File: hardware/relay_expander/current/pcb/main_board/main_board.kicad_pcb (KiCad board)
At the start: 2 copper layers, 130 x 85 mm, 83 parts, among them J1 Conn_01x07_Socket, J10 Screw_Terminal_01x02, J11 Screw_Terminal_01x02, J12 Screw_Terminal_01x02, J13 Screw_Terminal_01x02, J14 Screw_Terminal_01x02, J15 Screw_Terminal_01x02, J16 Screw_Terminal_01x02, J2 Conn_01x07_Socket, J3 Conn_01x02_Socket, J4 Screw_Terminal_01x02, J5 Screw_Terminal_01x02, J6 Screw_Terminal_01x02, J7 Screw_Terminal_01x02, J8 Screw_Terminal_01x02, J9 Screw_Terminal_01x02, K1 SANYOU_SRD_Form_C, K2 SANYOU_SRD_Form_C, K3 SANYOU_SRD_Form_C, K4 SANYOU_SRD_Form_C, K5 SANYOU_SRD_Form_C, K6 SANYOU_SRD_Form_C, K7 SANYOU_SRD_Form_C, K8 SANYOU_SRD_Form_C, U1 MCP23017x-x-SO, U2 ULN2803A, U3 TCMT4100, U4 TCMT4100, U5 TSR1-2433E

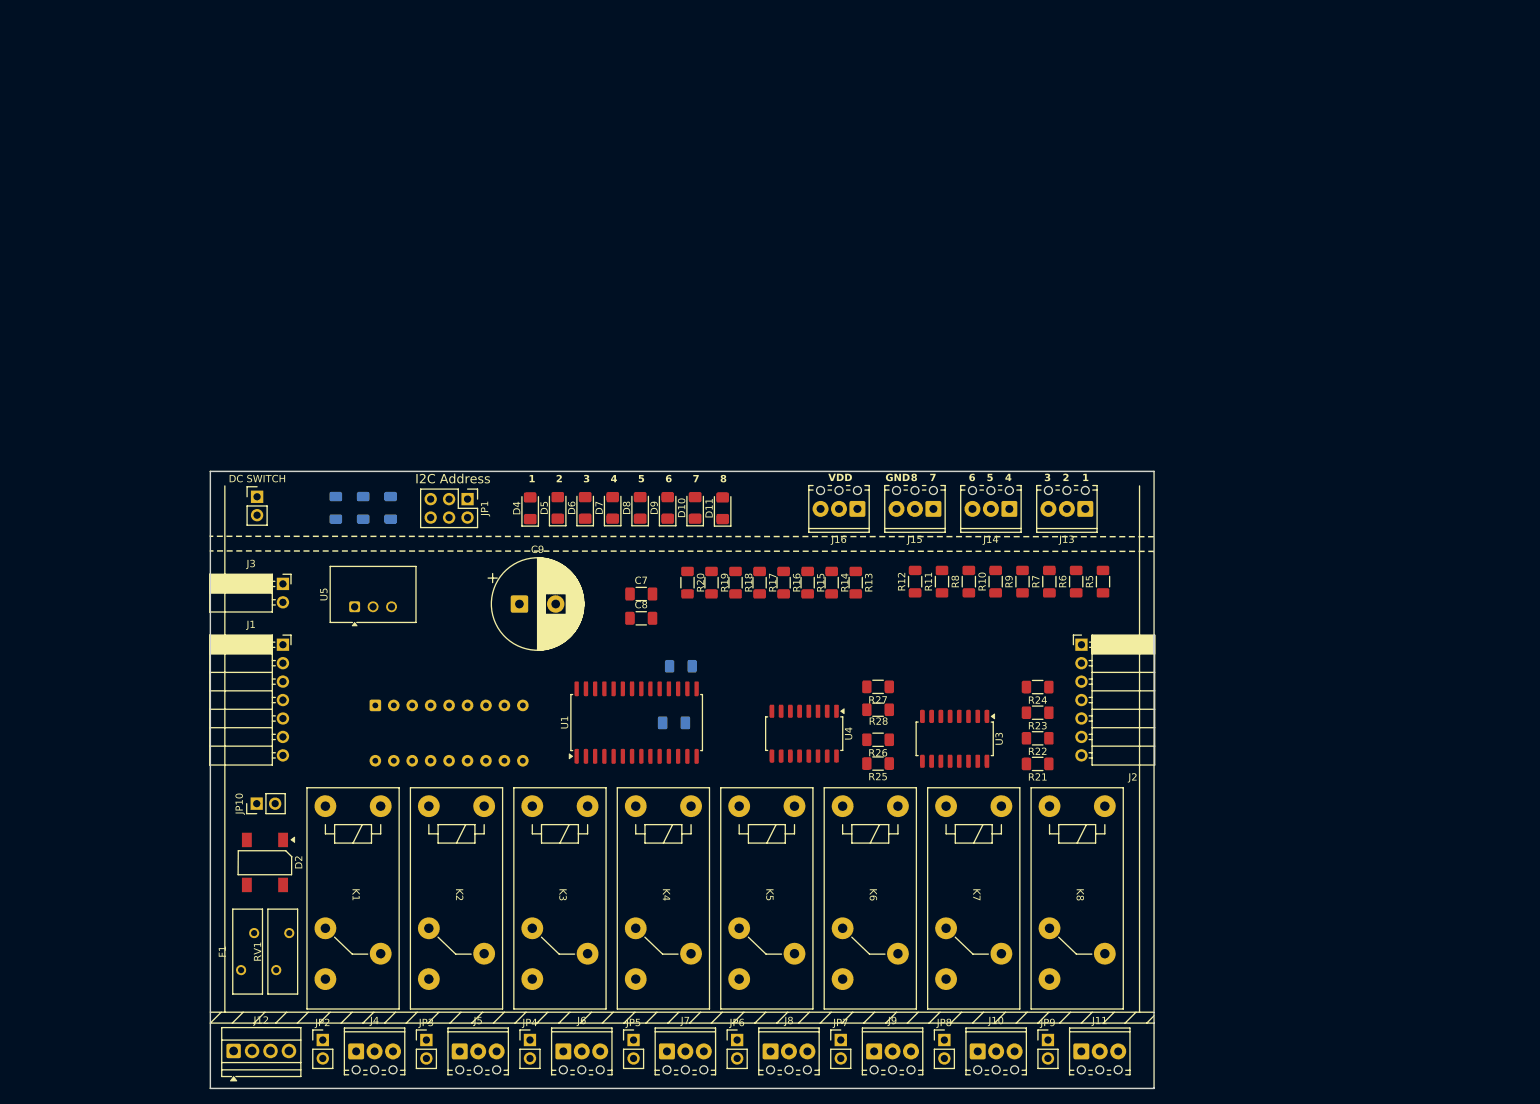
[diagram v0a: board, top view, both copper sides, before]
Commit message: [ADD] lauout for relay expander pcb
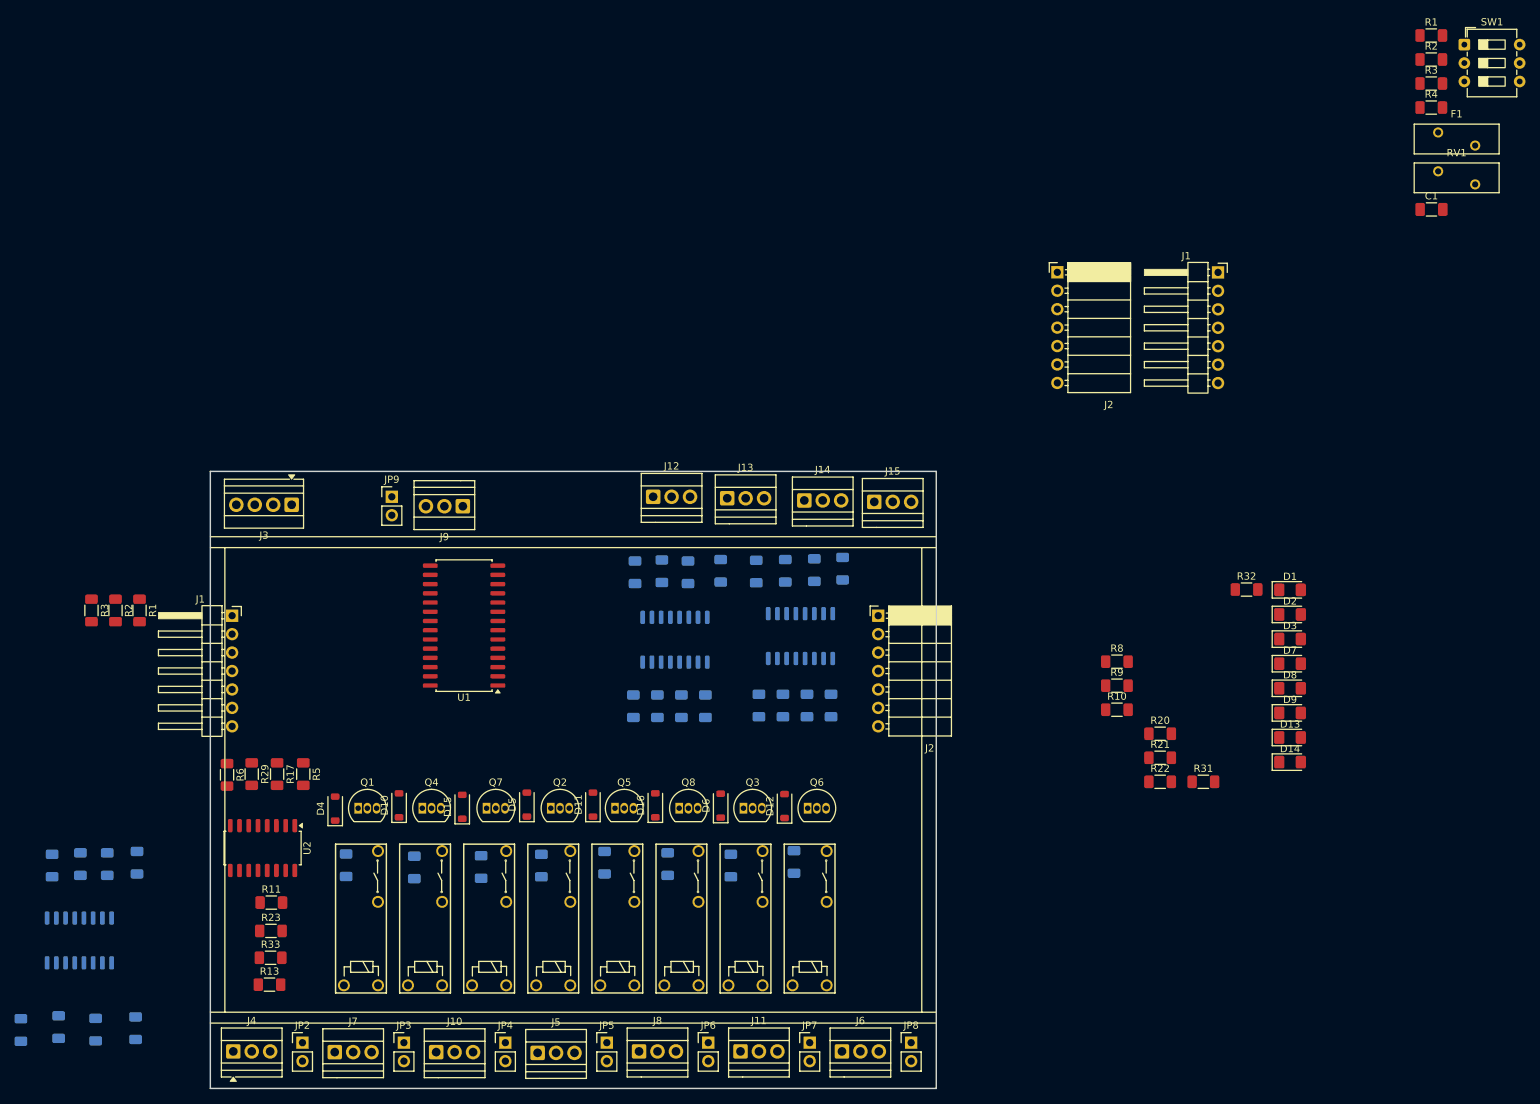
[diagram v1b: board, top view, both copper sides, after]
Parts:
- removed C7, C8: 22uF, Capacitor_SMD:C_1206_3216Metric_Pad1.33x1.80mm_HandSolder
- removed C9: 1000uF, Capacitor_THT:CP_Radial_D12.5mm_P5.00mm
- removed J16: Screw_Terminal_01x02, Project_Parts_Footprints_Lib:TerminalBlock_Phoenix_MPT-0,5-3-2.54_1x03_P2.54mm_Horizontal
- removed JP1: ~, Connector_PinHeader_2.54mm:PinHeader_2x03_P2.54mm_Vertical
- removed JP10: DC IN 6 - 36V, Connector_PinHeader_2.54mm:PinHeader_1x02_P2.54mm_Vertical
- removed JP13: DC SWITCH, Connector_PinHeader_2.54mm:PinHeader_1x02_P2.54mm_Vertical
- removed the R1 at (109.8, 57.5)
- removed the R2 at (106.1, 57.5)
- removed the R3 at (102.3, 57.5)
- added D1: LED, LED_SMD:LED_1206_3216Metric_Pad1.42x1.75mm_HandSolder, F.Cu at (233.7, 68.8)
- added D12: 1N4148, Diode_SMD:D_SOD-123, F.Cu at (164.1, 98.6)
- added D13: LED, LED_SMD:LED_1206_3216Metric_Pad1.42x1.75mm_HandSolder, F.Cu at (233.7, 89.2)
- added D14: LED, LED_SMD:LED_1206_3216Metric_Pad1.42x1.75mm_HandSolder, F.Cu at (233.7, 92.5)
- added D15: 1N4148, Diode_SMD:D_SOD-123, F.Cu at (119.7, 98.7)
- added D16: 1N4148, Diode_SMD:D_SOD-123, F.Cu at (146.3, 98.5)
- added D3: LED, LED_SMD:LED_1206_3216Metric_Pad1.42x1.75mm_HandSolder, F.Cu at (233.7, 75.6)
- added J1: Conn_01x07_Socket, homeautomation_core:PinHeader_1x07_P2.54mm_Horizontal_left, F.Cu at (223.8, 32.7)
- added J2: Conn_01x07_Socket, homeautomation_core:PinSocket_1x07_P2.54mm_Horizontal_Right, F.Cu at (201.7, 32.7)
- added Q1: BC548, Package_TO_SOT_THT:TO-92_Inline, F.Cu at (105.4, 98.9)
- added Q2: BC548, Package_TO_SOT_THT:TO-92_Inline, F.Cu at (131.9, 98.9)
- added Q3: BC548, Package_TO_SOT_THT:TO-92_Inline, F.Cu at (158.4, 98.9)
- added Q4: BC548, Package_TO_SOT_THT:TO-92_Inline, F.Cu at (114.2, 98.9)
- added Q5: BC548, Package_TO_SOT_THT:TO-92_Inline, F.Cu at (140.7, 98.9)
- added Q6: BC548, Package_TO_SOT_THT:TO-92_Inline, F.Cu at (167.3, 98.9)
- added Q7: BC548, Package_TO_SOT_THT:TO-92_Inline, F.Cu at (123.1, 98.9)
- added Q8: BC548, Package_TO_SOT_THT:TO-92_Inline, F.Cu at (149.6, 98.9)
- added R1: 10k, Resistor_SMD:R_1206_3216Metric_Pad1.30x1.75mm_HandSolder, F.Cu at (75.2, 71.7)
- added R1: 10k, Resistor_SMD:R_1206_3216Metric_Pad1.30x1.75mm_HandSolder, F.Cu at (253.2, -7.54)
- added R2: 10k, Resistor_SMD:R_1206_3216Metric_Pad1.30x1.75mm_HandSolder, F.Cu at (253.2, -4.24)
- added R2: 10k, Resistor_SMD:R_1206_3216Metric_Pad1.30x1.75mm_HandSolder, F.Cu at (71.9, 71.7)
- added R29: R470, Resistor_SMD:R_1206_3216Metric_Pad1.30x1.75mm_HandSolder, F.Cu at (90.7, 94.2)
- added R3: 10k, Resistor_SMD:R_1206_3216Metric_Pad1.30x1.75mm_HandSolder, F.Cu at (68.6, 71.7)
- added R3: 10k, Resistor_SMD:R_1206_3216Metric_Pad1.30x1.75mm_HandSolder, F.Cu at (253.2, -0.93)
- added R30: R470, Resistor_SMD:R_1206_3216Metric_Pad1.30x1.75mm_HandSolder, B.Cu at (67.1, 106.6)
- added R31: 1k, Resistor_SMD:R_1206_3216Metric_Pad1.30x1.75mm_HandSolder, F.Cu at (221.8, 95.3)
- added R32: 1k, Resistor_SMD:R_1206_3216Metric_Pad1.30x1.75mm_HandSolder, F.Cu at (227.7, 68.8)
- added R33: R4,7k, Resistor_SMD:R_1206_3216Metric_Pad1.30x1.75mm_HandSolder, F.Cu at (93.3, 119.5)
- added R34: R10k, Resistor_SMD:R_1206_3216Metric_Pad1.30x1.75mm_HandSolder, B.Cu at (122.3, 107.0)
- added R35: R4,7k, Resistor_SMD:R_1206_3216Metric_Pad1.30x1.75mm_HandSolder, B.Cu at (64.1, 129.1)
- added R36: R10k, Resistor_SMD:R_1206_3216Metric_Pad1.30x1.75mm_HandSolder, B.Cu at (139.3, 106.4)
- added R37: 1k, Resistor_SMD:R_1206_3216Metric_Pad1.30x1.75mm_HandSolder, B.Cu at (143.5, 66.4)
- added R38: 1k, Resistor_SMD:R_1206_3216Metric_Pad1.30x1.75mm_HandSolder, B.Cu at (147.2, 66.2)
- added R39: 1k, Resistor_SMD:R_1206_3216Metric_Pad1.30x1.75mm_HandSolder, B.Cu at (150.8, 66.4)
- added R40: 1k, Resistor_SMD:R_1206_3216Metric_Pad1.30x1.75mm_HandSolder, B.Cu at (155.3, 66.2)
- added R41: 1k, Resistor_SMD:R_1206_3216Metric_Pad1.30x1.75mm_HandSolder, B.Cu at (160.2, 66.3)
- added R42: 1k, Resistor_SMD:R_1206_3216Metric_Pad1.30x1.75mm_HandSolder, B.Cu at (164.2, 66.2)
- added R43: 1k, Resistor_SMD:R_1206_3216Metric_Pad1.30x1.75mm_HandSolder, B.Cu at (168.2, 66.1)
- added R44: 1k, Resistor_SMD:R_1206_3216Metric_Pad1.30x1.75mm_HandSolder, B.Cu at (172.1, 65.9)
- added R45: 10k, Resistor_SMD:R_1206_3216Metric_Pad1.30x1.75mm_HandSolder, B.Cu at (143.3, 84.8)
- added R46: 10k, Resistor_SMD:R_1206_3216Metric_Pad1.30x1.75mm_HandSolder, B.Cu at (146.6, 84.8)
- added R47: 10k, Resistor_SMD:R_1206_3216Metric_Pad1.30x1.75mm_HandSolder, B.Cu at (149.9, 84.8)
- added R48: 10k, Resistor_SMD:R_1206_3216Metric_Pad1.30x1.75mm_HandSolder, B.Cu at (153.2, 84.8)
- added R49: 10k, Resistor_SMD:R_1206_3216Metric_Pad1.30x1.75mm_HandSolder, B.Cu at (160.6, 84.8)
- added R50: 10k, Resistor_SMD:R_1206_3216Metric_Pad1.30x1.75mm_HandSolder, B.Cu at (163.9, 84.8)
- added R51: 10k, Resistor_SMD:R_1206_3216Metric_Pad1.30x1.75mm_HandSolder, B.Cu at (167.2, 84.8)
- added R52: 10k, Resistor_SMD:R_1206_3216Metric_Pad1.30x1.75mm_HandSolder, B.Cu at (170.5, 84.8)
- added SW1: SW_DIP_x03, Button_Switch_THT:SW_DIP_SPSTx03_Slide_6.7x9.18mm_W7.62mm_P2.54mm_LowProfile, F.Cu at (257.7, -6.29)
- C1, R4: moved to F.Cu
- D10, D11, D4, D5, D6: value LED -> 1N4148; footprint LED_SMD:LED_1206_3216Metric_Pad1.42x1.75mm_HandSolder -> Diode_SMD:D_SOD-123
- D2: value DB157S -> LED; footprint Wojtek_lib_footprints:DB157S -> LED_SMD:LED_1206_3216Metric_Pad1.42x1.75mm_HandSolder
- J1: footprint templates_lib_footprints:PinSocket_1x07_P2.54mm_Horizontal -> homeautomation_core:PinHeader_1x07_P2.54mm_Horizontal_left
- J10, J11, J13, J14, J15, J5, J6, J7, J9: footprint Project_Parts_Footprints_Lib:TerminalBlock_Phoenix_MPT-0,5-3-2.54_1x03_P2.54mm_Horizontal -> footprints:Terminal_block_1x3_2,54
- J12: footprint TerminalBlock:TerminalBlock_Xinya_XY308-2.54-4P_1x04_P2.54mm_Horizontal -> footprints:Terminal_block_1x3_2,54
- J2: footprint templates_lib_footprints:PinSocket_1x07_P2.54mm_Horizontal_Right -> homeautomation_core:PinSocket_1x07_P2.54mm_Horizontal_Right
- J3: value Conn_01x02_Socket -> Screw_Terminal_01x02; footprint Connector_PinSocket_2.54mm:PinSocket_1x02_P2.54mm_Horizontal -> TerminalBlock:TerminalBlock_Xinya_XY308-2.54-4P_1x04_P2.54mm_Horizontal
- J4: footprint Project_Parts_Footprints_Lib:TerminalBlock_Phoenix_MPT-0,5-3-2.54_1x03_P2.54mm_Horizontal -> TerminalBlock:TerminalBlock_Xinya_XY308-2.54-3P_1x03_P2.54mm_Horizontal
- J8: value Screw_Terminal_01x02 -> Screw_Terminal_01x03; footprint Project_Parts_Footprints_Lib:TerminalBlock_Phoenix_MPT-0,5-3-2.54_1x03_P2.54mm_Horizontal -> footprints:Terminal_block_1x3_2,54
- K1, K2, K3, K4, K5, K6, K7, K8: value SANYOU_SRD_Form_C -> HF46F-12-HS1; footprint templates_lib_footprints:Songle_SMI-SL-A -> homeautomation_core:relay_HF46F
- R11, R13: value 1k -> R4,7k
- R12, R14, R16: value 1k -> R10k; moved to B.Cu
- R15: value 1k -> R4,7k; moved to B.Cu
- R17, R5, R6: value 1k -> R470
- R18, R19, R7: value 1k -> R470; moved to B.Cu
- R21, R22: value 10k -> 1k
- R23: value 10k -> R4,7k
- R24, R26, R28: value 10k -> R10k; moved to B.Cu
- R25, R27: value 10k -> R4,7k; moved to B.Cu
- U2: value ULN2803A -> TCMT4100; footprint Package_DIP:DIP-18_W7.62mm -> Package_SO:SOP-16_4.4x10.4mm_P1.27mm; moved to F.Cu
- U3, U4: moved to B.Cu
- U5: value TSR1-2433E -> TCMT4100; footprint Converter_DCDC:Converter_DCDC_TRACO_TSR1-xxxxE_THT -> Package_SO:SOP-16_4.4x10.4mm_P1.27mm; moved to B.Cu
- moved F1 201.3 mm to (254.1, 5.82), turned to 0 degrees
- moved RV1 194.2 mm to (254.1, 11.2), turned to 0 degrees
- moved D2 145.3 mm to (233.7, 72.2), turned to 0 degrees
- moved R7 135.5 mm to (70.8, 106.6), turned to -90 degrees
- moved R4 128.9 mm to (253.2, 2.38)
- moved C1 126.1 mm to (253.2, 16.4), turned to 0 degrees
- moved U3 123.7 mm to (67.0, 117.1)
- moved R25 123.7 mm to (58.9, 129.4), turned to -90 degrees
- moved R6 120.0 mm to (87.3, 94.3), turned to -90 degrees
- moved JP9 117.3 mm to (110.0, 56.0)
- moved R15 115.8 mm to (69.2, 129.4)
- moved R5 113.3 mm to (97.8, 94.2), turned to -90 degrees
- moved R27 112.6 mm to (74.7, 129.2), turned to -90 degrees
- moved R23 109.8 mm to (93.3, 115.8), turned to 0 degrees
- moved R11 102.4 mm to (93.4, 111.9), turned to 0 degrees
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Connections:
- D10 pad 1: /Relays/RELAY_7 -> +12V
- D11 pad 1: /Relays/RELAY_8 -> +12V
- D2 pad 1: Net-(D2-+) -> Net-(D2-K)
- D2 pad 2: GND_Power_Supply -> Net-(D2-A)
- D4 pad 1: /Relays/RELAY_1 -> +12V
- D4 pad 2: Net-(D4-A) -> Net-(D1-K)
- D5 pad 1: /Relays/RELAY_2 -> +12V
- D5 pad 2: Net-(D5-A) -> Net-(D2-K)
- D6 pad 1: /Relays/RELAY_3 -> +12V
- D6 pad 2: Net-(D6-A) -> Net-(D3-K)
- D7 pad 1: /Relays/RELAY_4 -> Net-(D10-A)
- D8 pad 1: /Relays/RELAY_5 -> Net-(D11-A)
- D9 pad 1: /Relays/RELAY_6 -> Net-(D12-A)
- F1 pad 1: Net-(J12-Pin_3) -> Net-(J3-Pin_1)
- F1 pad 2: 24VAC -> L1
- J1 pad 6: VDD -> GND_2
- J1 pad 7: GND_2 -> +12V
- J12 pad 1: L2 -> Net-(J12-Pin_1)
- J12 pad 2: L2 -> Net-(J12-Pin_2)
- J14 pad 3: Net-(J14-Pin_3) -> GND_2
- J15 pad 1: GND_2 -> +12V
- J15 pad 2: Net-(J15-Pin_2) -> +12V
- J15 pad 3: Net-(J15-Pin_3) -> +12V
- J2 pad 6: VDD -> GND_2
- J2 pad 7: GND_2 -> +12V
- J3 pad 1: GND_Power_Supply -> Net-(J3-Pin_1)
- J3 pad 2: +5V_Power_Supply -> L2
- JP2 pad 2: 24VAC -> L1
- JP3 pad 2: 24VAC -> L1
- JP4 pad 2: 24VAC -> L1
- JP5 pad 2: 24VAC -> L1
- JP6 pad 2: 24VAC -> L1
- JP7 pad 2: 24VAC -> L1
- JP8 pad 2: 24VAC -> L1
- JP9 pad 2: 24VAC -> L1
- K1 pad 1: Net-(J4-Pin_3) -> Net-(D1-K)
- K1 pad 2: /Relays/RELAY_1 -> +12V
- K1 pad 3: Net-(J4-Pin_2) -> Net-(J4-Pin_3)
- K1 pad 4: (no net) -> Net-(J4-Pin_2)
- K2 pad 1: Net-(J5-Pin_3) -> Net-(D2-K)
- K2 pad 2: /Relays/RELAY_2 -> +12V
- K2 pad 3: Net-(J5-Pin_2) -> Net-(J5-Pin_3)
- K2 pad 4: (no net) -> Net-(J5-Pin_2)
- K3 pad 1: Net-(J6-Pin_3) -> Net-(D3-K)
- K3 pad 2: /Relays/RELAY_3 -> +12V
- K3 pad 3: Net-(J6-Pin_2) -> Net-(J6-Pin_3)
- K3 pad 4: (no net) -> Net-(J6-Pin_2)
- K4 pad 1: Net-(J7-Pin_3) -> Net-(D10-A)
- K4 pad 2: /Relays/RELAY_4 -> +12V
- K4 pad 3: Net-(J7-Pin_2) -> Net-(J7-Pin_3)
- K4 pad 4: (no net) -> Net-(J7-Pin_2)
- K5 pad 1: Net-(J8-Pin_3) -> Net-(D11-A)
- K5 pad 2: /Relays/RELAY_5 -> +12V
- K5 pad 3: Net-(J8-Pin_2) -> Net-(J8-Pin_3)
- K5 pad 4: (no net) -> Net-(J8-Pin_2)
- K6 pad 1: Net-(J9-Pin_3) -> Net-(D12-A)
- K6 pad 2: /Relays/RELAY_6 -> +12V
- K6 pad 3: Net-(J9-Pin_2) -> Net-(J9-Pin_3)
- K6 pad 4: (no net) -> Net-(J9-Pin_2)
- K7 pad 1: Net-(J10-Pin_3) -> Net-(D13-K)
- K7 pad 2: /Relays/RELAY_7 -> +12V
- K7 pad 3: Net-(J10-Pin_2) -> Net-(J10-Pin_3)
- K7 pad 4: (no net) -> Net-(J10-Pin_2)
- K8 pad 1: Net-(J11-Pin_3) -> Net-(D14-K)
- K8 pad 2: /Relays/RELAY_8 -> +12V
- K8 pad 3: Net-(J11-Pin_2) -> Net-(J11-Pin_3)
- K8 pad 4: (no net) -> Net-(J11-Pin_2)
- R10 pad 1: Net-(R10-Pad1) -> Net-(D3-A)
- R10 pad 2: Net-(J14-Pin_1) -> +12V
- R11 pad 2: Net-(J15-Pin_3) -> Net-(Q1-B)
- R12 pad 1: Net-(R12-Pad1) -> Net-(Q1-B)
- R12 pad 2: Net-(J15-Pin_2) -> GND_2
- R13 pad 1: Net-(D4-A) -> Net-(R13-Pad1)
- R13 pad 2: VDD -> Net-(Q2-B)
- R14 pad 1: Net-(D5-A) -> Net-(Q2-B)
- R14 pad 2: VDD -> GND_2
- R15 pad 1: Net-(D6-A) -> Net-(R15-Pad1)
- R15 pad 2: VDD -> Net-(Q3-B)
- R16 pad 1: Net-(D7-A) -> Net-(Q3-B)
- R16 pad 2: VDD -> GND_2
- R17 pad 1: Net-(D8-A) -> /Relays/RELAY_2
- R17 pad 2: VDD -> Net-(R17-Pad2)
- R18 pad 1: Net-(D9-A) -> /Relays/RELAY_5
- R18 pad 2: VDD -> Net-(R18-Pad2)
- R19 pad 1: Net-(D10-A) -> /Relays/RELAY_8
- R19 pad 2: VDD -> Net-(R19-Pad2)
- R20 pad 1: Net-(D11-A) -> Net-(D7-A)
- R20 pad 2: VDD -> +12V
- R21 pad 1: +3V3 -> Net-(D8-A)
- R21 pad 2: /Digital_Inputs/In_0 -> +12V
- R22 pad 1: +3V3 -> Net-(D9-A)
- R22 pad 2: /Digital_Inputs/In_1 -> +12V
- R23 pad 1: +3V3 -> Net-(R23-Pad1)
- R23 pad 2: /Digital_Inputs/In_2 -> Net-(Q4-B)
- R24 pad 1: +3V3 -> Net-(Q4-B)
- R24 pad 2: /Digital_Inputs/In_3 -> GND_2
- R25 pad 1: +3V3 -> Net-(R25-Pad1)
- R25 pad 2: /Digital_Inputs/In_4 -> Net-(Q5-B)
- R26 pad 1: +3V3 -> Net-(Q5-B)
- R26 pad 2: /Digital_Inputs/In_5 -> GND_2
- R27 pad 1: +3V3 -> Net-(R27-Pad1)
- R27 pad 2: /Digital_Inputs/In_6 -> Net-(Q6-B)
- R28 pad 1: +3V3 -> Net-(Q6-B)
- R28 pad 2: /Digital_Inputs/In_7 -> GND_2
- R4 pad 1: Net-(U1-~{RESET}) -> +3V3
- R4 pad 2: +3V3 -> /ADDR_A2
- R5 pad 1: Net-(R5-Pad1) -> /Relays/RELAY_1
- R5 pad 2: Net-(J13-Pin_3) -> Net-(R5-Pad2)
- R6 pad 1: Net-(R6-Pad1) -> /Relays/RELAY_4
- R6 pad 2: Net-(J13-Pin_2) -> Net-(R6-Pad2)
- R7 pad 1: Net-(R7-Pad1) -> /Relays/RELAY_7
- R7 pad 2: Net-(J13-Pin_1) -> Net-(R7-Pad2)
- R8 pad 1: Net-(R8-Pad1) -> Net-(D1-A)
- R8 pad 2: Net-(J14-Pin_3) -> +12V
- R9 pad 1: Net-(R9-Pad1) -> Net-(D2-A)
- R9 pad 2: Net-(J14-Pin_2) -> +12V
- RV1 pad 1: 24VAC -> L1
- U1 pad 1: Net-(U1-GPB0) -> /Relays/RELAY_1
- U1 pad 2: Net-(U1-GPB1) -> /Relays/RELAY_2
- U1 pad 3: Net-(U1-GPB2) -> /Relays/RELAY_3
- U1 pad 4: Net-(U1-GPB3) -> /Relays/RELAY_4
- U1 pad 5: Net-(U1-GPB4) -> /Relays/RELAY_5
- U1 pad 6: Net-(U1-GPB5) -> /Relays/RELAY_6
- U1 pad 7: Net-(U1-GPB6) -> /Relays/RELAY_7
- U1 pad 8: Net-(U1-GPB7) -> /Relays/RELAY_8
- U2 pad 1: Net-(U1-GPB0) -> Net-(R5-Pad2)
- U2 pad 10: VDD -> +12V
- U2 pad 11: /Relays/RELAY_8 -> Net-(R33-Pad1)
- U2 pad 12: /Relays/RELAY_7 -> +12V
- U2 pad 13: /Relays/RELAY_6 -> Net-(R23-Pad1)
- U2 pad 14: /Relays/RELAY_5 -> +12V
- U2 pad 15: /Relays/RELAY_4 -> Net-(R11-Pad1)
- U2 pad 16: /Relays/RELAY_3 -> +12V
- U2 pad 2: Net-(U1-GPB1) -> GND
- U2 pad 3: Net-(U1-GPB2) -> Net-(R17-Pad2)
- U2 pad 4: Net-(U1-GPB3) -> GND
- U2 pad 5: Net-(U1-GPB4) -> Net-(R29-Pad2)
- U2 pad 6: Net-(U1-GPB5) -> GND
- U2 pad 7: Net-(U1-GPB6) -> Net-(R6-Pad2)
- U2 pad 8: Net-(U1-GPB7) -> GND
- U2 pad 9: GND_2 -> Net-(R13-Pad1)
- U3 pad 1: Net-(R5-Pad1) -> Net-(R18-Pad2)
- U3 pad 10: /Digital_Inputs/In_3 -> +12V
- U3 pad 11: GND -> Net-(R15-Pad1)
- U3 pad 12: /Digital_Inputs/In_2 -> +12V
- U3 pad 13: GND -> Net-(R35-Pad1)
- U3 pad 14: /Digital_Inputs/In_1 -> +12V
- U3 pad 15: GND -> Net-(R25-Pad1)
- U3 pad 16: /Digital_Inputs/In_0 -> +12V
- U3 pad 2: GND_2 -> GND
- U3 pad 3: Net-(R6-Pad1) -> Net-(R30-Pad2)
- U3 pad 4: GND_2 -> GND
- U3 pad 5: Net-(R7-Pad1) -> Net-(R7-Pad2)
- U3 pad 6: GND_2 -> GND
- U3 pad 7: Net-(R8-Pad1) -> Net-(R19-Pad2)
- U3 pad 8: GND_2 -> GND
- U3 pad 9: GND -> Net-(R27-Pad1)
- U4 pad 1: Net-(R9-Pad1) -> Net-(R37-Pad1)
- U4 pad 10: /Digital_Inputs/In_7 -> /Digital_Inputs/In_3
- U4 pad 12: /Digital_Inputs/In_6 -> /Digital_Inputs/In_2
- U4 pad 14: /Digital_Inputs/In_5 -> /Digital_Inputs/In_1
- U4 pad 16: /Digital_Inputs/In_4 -> /Digital_Inputs/In_0
- U4 pad 3: Net-(R10-Pad1) -> Net-(R38-Pad1)
- U4 pad 5: Net-(R11-Pad1) -> Net-(R39-Pad1)
- U4 pad 7: Net-(R12-Pad1) -> Net-(R40-Pad1)
- U5 pad 2: GND -> GND_2
- U5 pad 3: +5V_Power_Supply -> Net-(R42-Pad1)
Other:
- board size 130 x 85 mm -> 100 x 85 mm
- board text removed: "1"
- board text removed: "2"
- board text removed: "3"
- board text removed: "4"
- board text removed: "5"
- board text removed: "6"
- board text removed: "7"
- board text removed: "8"
- board text removed: "GND"
- board text removed: "VDD"
